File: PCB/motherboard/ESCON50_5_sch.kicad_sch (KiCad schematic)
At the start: 27 parts, among them Q1 NMOS, Q2 PMOS, U6 LM74700QDBVTQ1, U9 TL431D

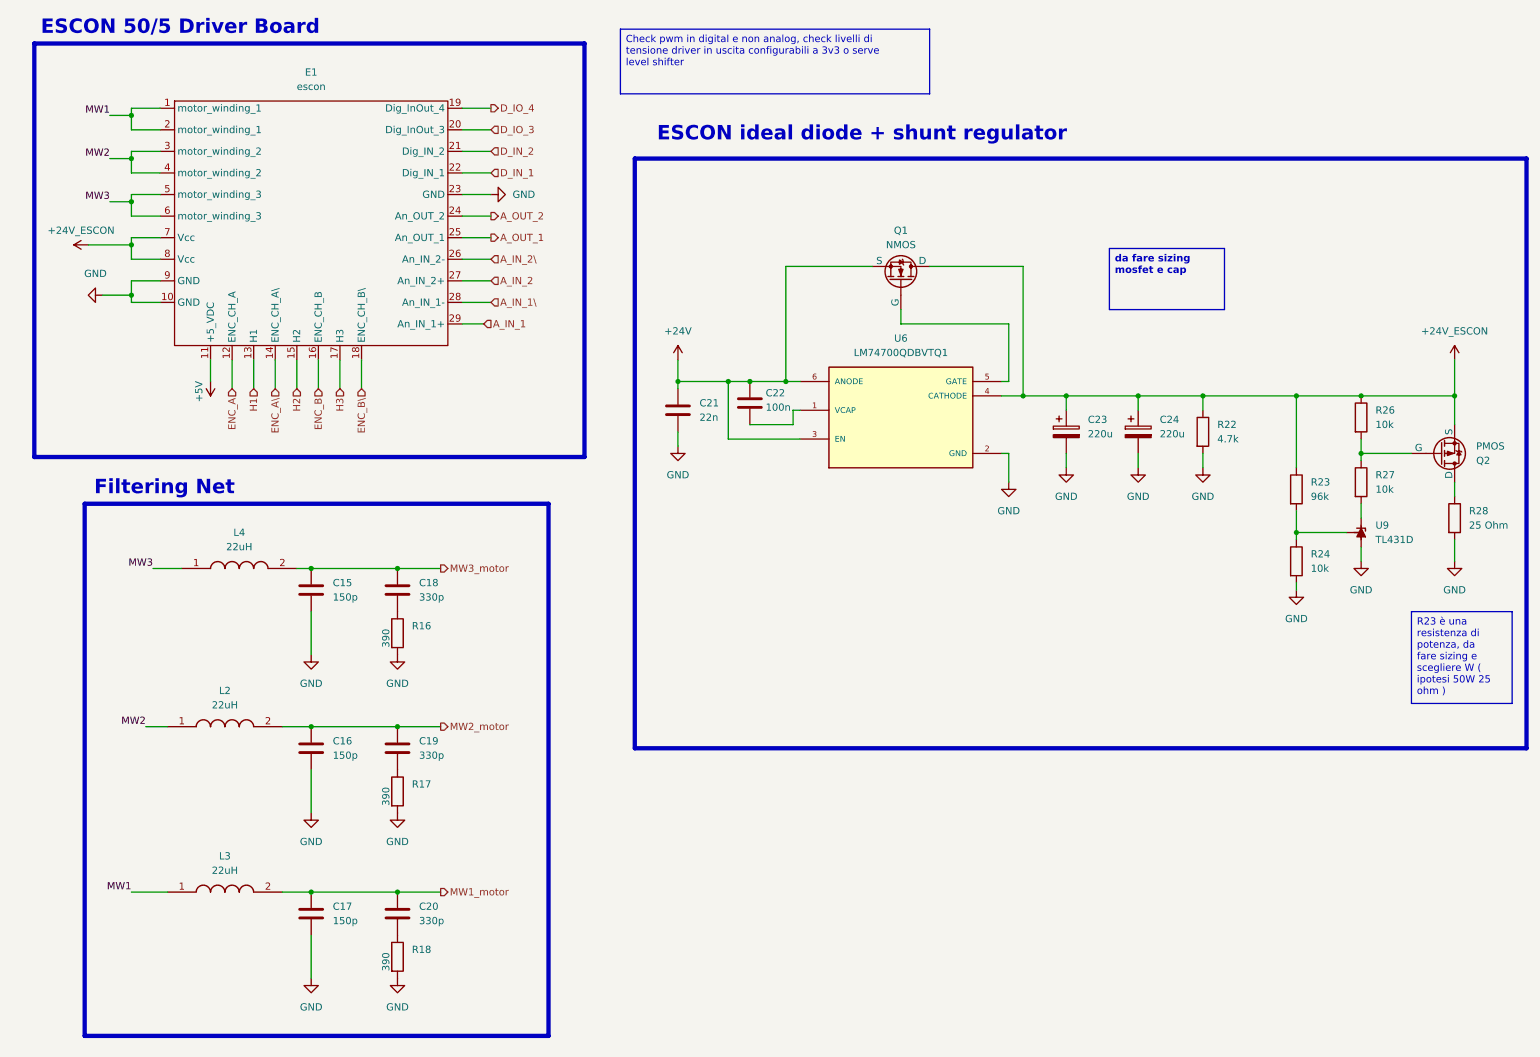
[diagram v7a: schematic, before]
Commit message: sizing schematics done
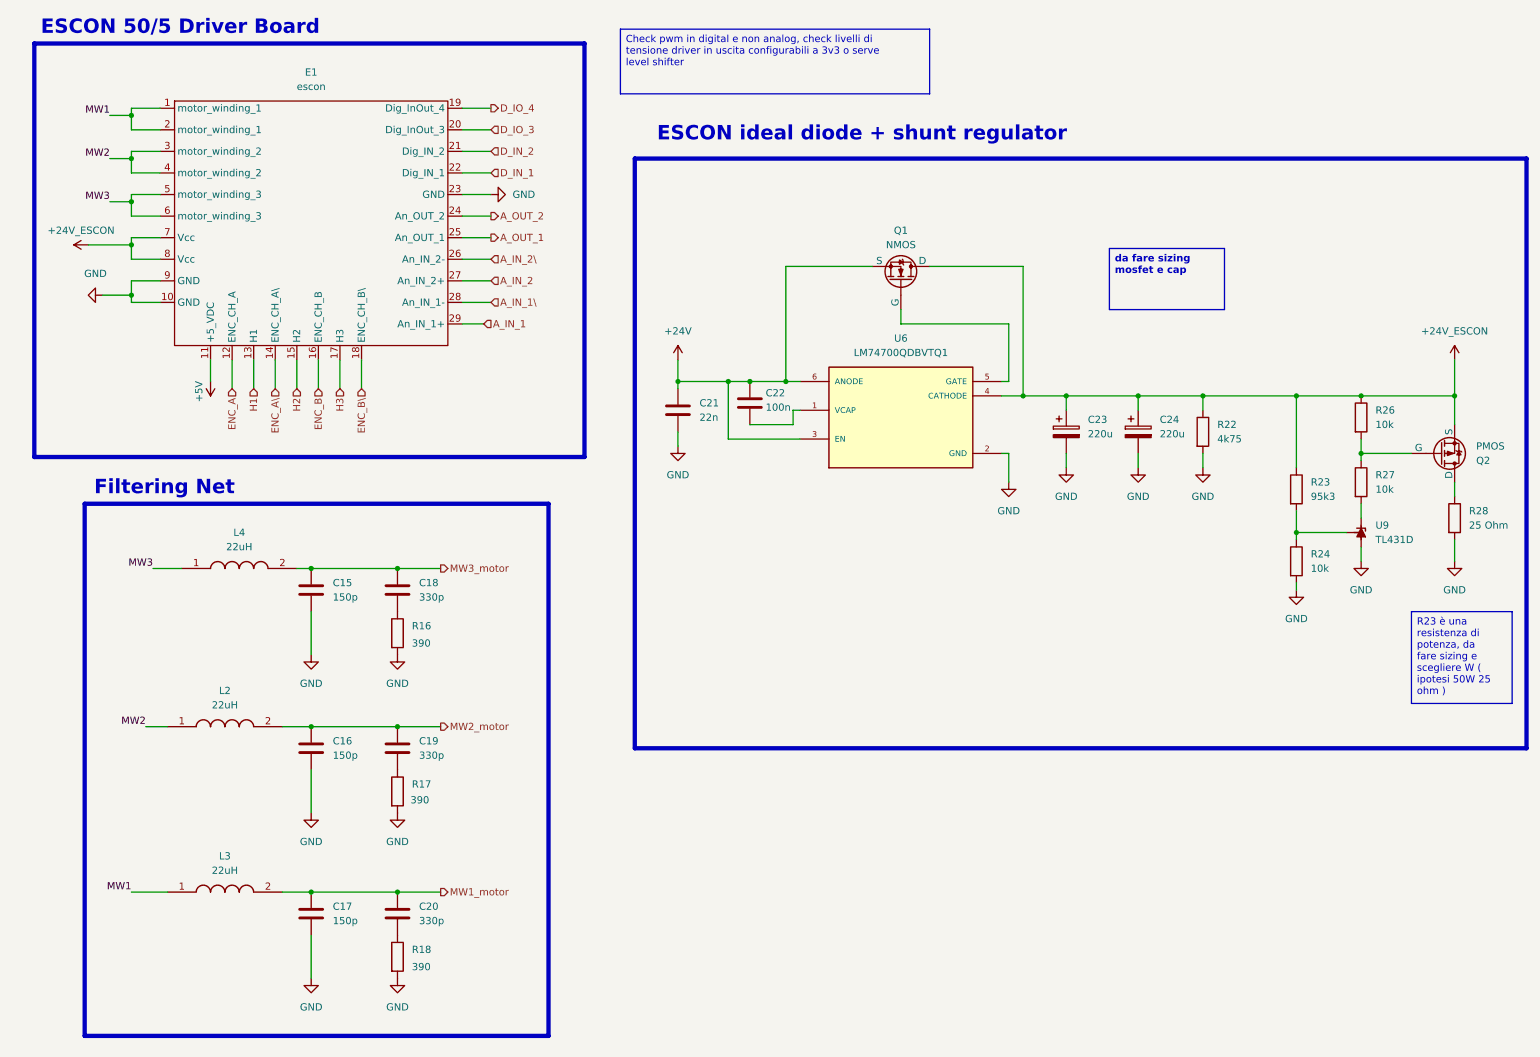
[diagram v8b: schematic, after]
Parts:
- R22: value 4.7k -> 4k75
- R23: value 96k -> 95k3
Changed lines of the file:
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@@
 		)
 		(property "Value" "390"
-			(at 79.248 181.61 90)
+			(at 83.82 180.848 0)
 			(show_name no)
 			(do_not_autoplace no)
@@
 		)
 		(property "Value" "390"
-			(at 79.248 152.4 90)
+			(at 83.566 151.384 0)
 			(show_name no)
 			(do_not_autoplace no)
@@
 		)
 		(property "Value" "390"
-			(at 79.248 124.46 90)
+			(at 83.82 123.698 0)
 			(show_name no)
 			(do_not_autoplace no)
@@
 			)
 		)
-		(property "Value" "96k"
+		(property "Value" "95k3"
 			(at 242.57 97.7899 0)
 			(show_name no)
@@
 			)
 		)
-		(property "Value" "4.7k"
+		(property "Value" "4k75"
 			(at 226.06 87.6299 0)
 			(show_name no)
